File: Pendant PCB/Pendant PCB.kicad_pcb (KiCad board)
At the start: 2 copper layers, 75 x 133 mm, 36 parts, among them J1 Conn_01x20, J2 Conn_01x20, J4 Conn_01x05, J5 Conn_02x02_Odd_Even

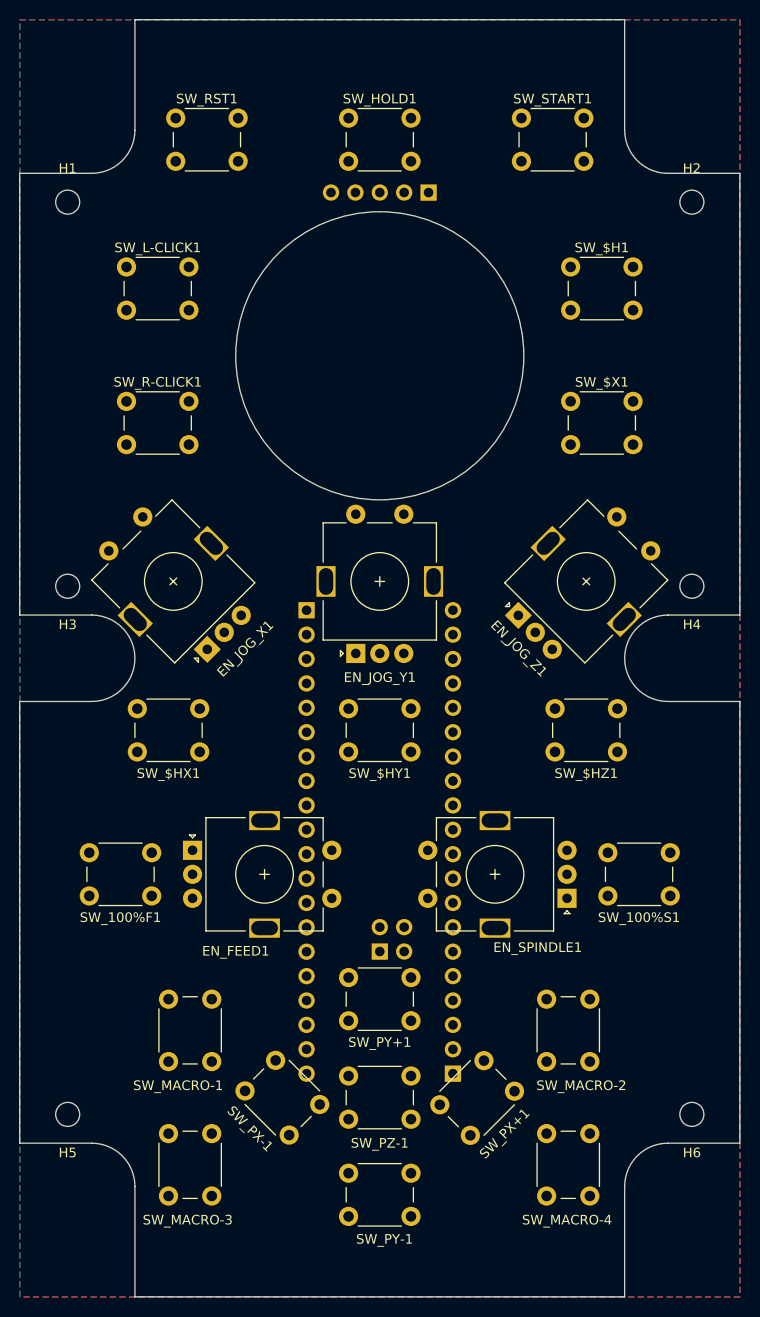
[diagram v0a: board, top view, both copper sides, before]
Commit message: PCB routed. Feed and Spindle encoders moved .5mm closer to Y-axis
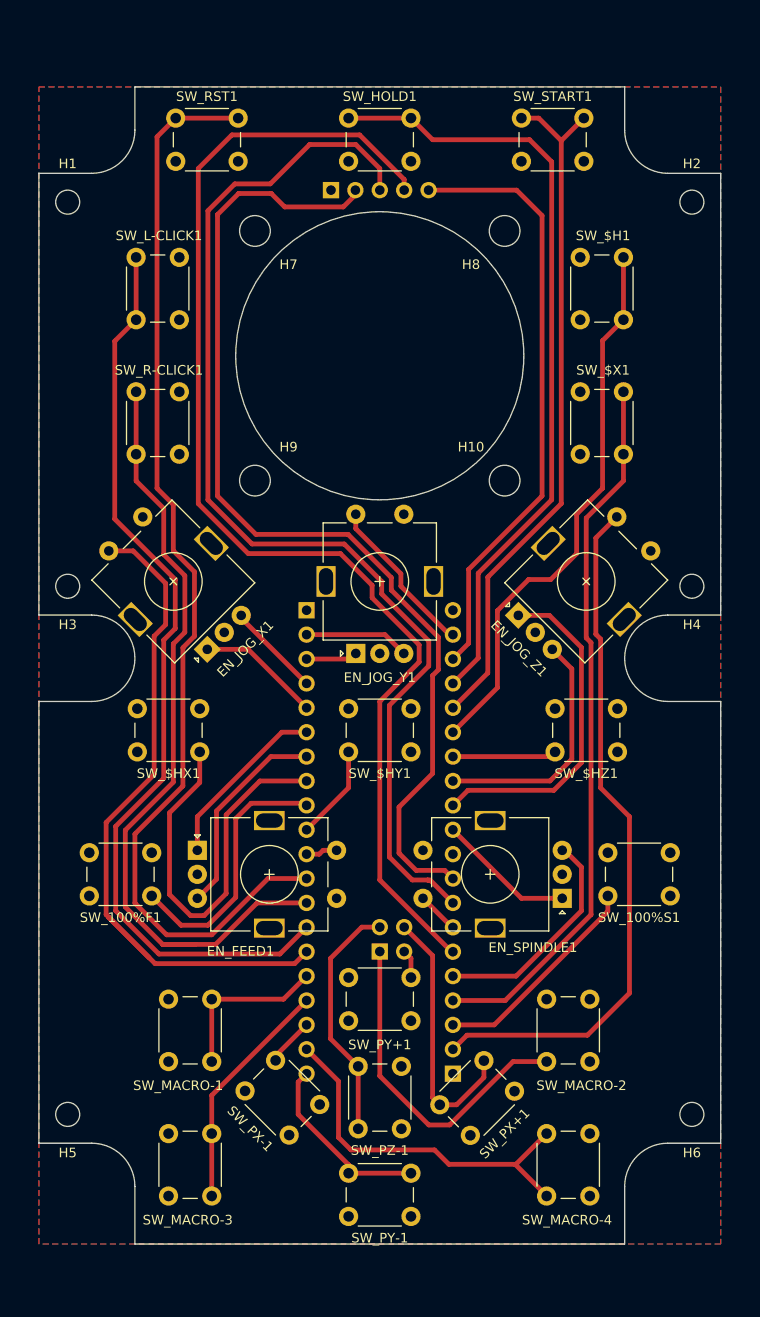
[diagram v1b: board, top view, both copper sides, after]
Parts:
- added H10: MountingHole, MountingHole:MountingHole_3.2mm_M3, F.Cu at (108.0, 81.5)
- added H7: MountingHole, MountingHole:MountingHole_3.2mm_M3, F.Cu at (82.0, 55.5)
- added H8: MountingHole, MountingHole:MountingHole_3.2mm_M3, F.Cu at (108.0, 55.5)
- added H9: MountingHole, MountingHole:MountingHole_3.2mm_M3, F.Cu at (82.0, 81.5)
- moved J4 10.2 mm to (89.9, 51.2), turned to 270 degrees
- moved SW_HOLD1 7.91 mm to (98.2, 48.2), turned to 180 degrees
- moved SW_PY+1 7.91 mm to (98.2, 137.8), turned to 180 degrees
- moved SW_$H1 5.59 mm to (120.4, 58.2), turned to 270 degrees
- moved SW_$X1 5.59 mm to (120.4, 72.2), turned to 270 degrees
- moved SW_PZ-1 5.59 mm to (97.2, 142.5), turned to 270 degrees
- moved SW_L-CLICK1 5.59 mm to (69.6, 64.8), turned to 90 degrees
- moved SW_R-CLICK1 5.59 mm to (69.6, 78.8), turned to 90 degrees
- moved EN_FEED1 0.50 mm to (83.5, 122.5)
- moved EN_SPINDLE1 0.50 mm to (106.5, 122.5)
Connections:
- net /38 renamed /A0
- EN_FEED1 pad B: /FB -> /4
- EN_FEED1 pad S2: /33 -> /8
- EN_JOG_X1 pad A: /1 -> /2
- EN_JOG_X1 pad B: /XB -> /1
- EN_JOG_X1 pad S2: /SW_X -> /12
- EN_JOG_Y1 pad B: /YB -> /27
- EN_JOG_Y1 pad S2: /SW_Y -> /26
- EN_JOG_Z1 pad B: /ZB -> /20
- EN_JOG_Z1 pad S2: /SW_Z -> /44
- EN_SPINDLE1 pad B: /SB -> /41
- EN_SPINDLE1 pad S2: /28 -> /39
- J2 pad 6: /40 -> /A2
- J4 pad 4: /39 -> /A2
- J4 pad 5: /J_SW -> /25
- SW_$H1 pad 1: GND -> /22
- SW_$H1 pad 2: /HA -> GND
- SW_$HX1 pad 2: /HX -> /5
- SW_$HY1 pad 2: /32 -> /7
- SW_$HZ1 pad 2: /HZ -> /21
- SW_$X1 pad 1: GND -> /42
- SW_$X1 pad 2: /UL -> GND
- SW_100%F1 pad 2: /FR -> /6
- SW_100%S1 pad 2: /SR -> /43
- SW_HOLD1 pad 2: /HLD -> /24
- SW_L-CLICK1 pad 1: GND -> /11
- SW_L-CLICK1 pad 2: /ML -> GND
- SW_MACRO-1 pad 2: /M1 -> /13
- SW_MACRO-2 pad 1: GND -> /33
- SW_MACRO-2 pad 2: /M2 -> GND
- SW_MACRO-3 pad 2: /M3 -> /14
- SW_MACRO-4 pad 1: GND -> /16
- SW_MACRO-4 pad 2: /M4 -> GND
- SW_PX+1 pad 1: GND -> /28
- SW_PX+1 pad 2: /PX+ -> GND
- SW_PX-1 pad 1: GND -> /15
- SW_PX-1 pad 2: /PX- -> GND
- SW_PY-1 pad 1: GND -> /17
- SW_PY-1 pad 2: /PY- -> GND
- SW_PZ-1 pad 2: /PZ- -> /32
- SW_R-CLICK1 pad 1: GND -> /10
- SW_R-CLICK1 pad 2: /MR -> GND
- SW_RST1 pad 1: GND -> /9
- SW_RST1 pad 2: /RST -> GND
- SW_START1 pad 1: GND -> /23
- SW_START1 pad 2: /STR -> GND
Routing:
- net /A2: track 0.00 -> 127.6 mm
- net /A0: track 0.00 -> 116.8 mm
- net /9: track 0.00 -> 114.9 mm
- net +5VA: track 0.00 -> 106.9 mm
- net /11: track 0.00 -> 97.0 mm
- net /10: track 0.00 -> 84.0 mm
- net /24: track 0.00 -> 81.6 mm
- net /42: track 0.00 -> 74.3 mm
- net /12: track 0.00 -> 73.9 mm
- net /44: track 0.00 -> 72.8 mm
- net /23: track 0.00 -> 72.2 mm
- net /25: track 0.00 -> 62.9 mm
- net /22: track 0.00 -> 58.2 mm
- net /5: track 0.00 -> 42.0 mm
- net /16: track 0.00 -> 39.4 mm
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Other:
- board size 75 x 133 mm -> 71 x 120.5 mm
- net class Default: clearance 0.3 -> 0.47
- rule pad_to_mask_clearance: 0 -> 0.05
- rule trace_clearance: 0.3 -> 0.47
